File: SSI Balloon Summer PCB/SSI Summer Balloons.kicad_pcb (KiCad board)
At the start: 4 copper layers, 80 x 59 mm, 106 parts, among them J1 Battery connector, J2 Conn_01x02, J3 LoRa antenna, J4 APRS antenna, J5 Conn_01x05, J6 1040310811, J7 GPS antenna, J8 PT1000 Sensor, J9 Camera, Q2 DMG2305UX-7, SW2 SW_SPST, SW3 SW_SPST, U1 RFM95W-915S2, U10 MS5611-01BA03, U11 TPS63070RNMR, U12 TPS63070RNMR, U3 AP2112K-3.3TRG1, U4 ICM-42688-P, U5 DRA818V, U7 STM32F411CEUx, U8 MAX-M10S-00B, U9 MAX31865ATP_T, Y1 ABM8W-12.0000MHZ-8-K1Z-T3

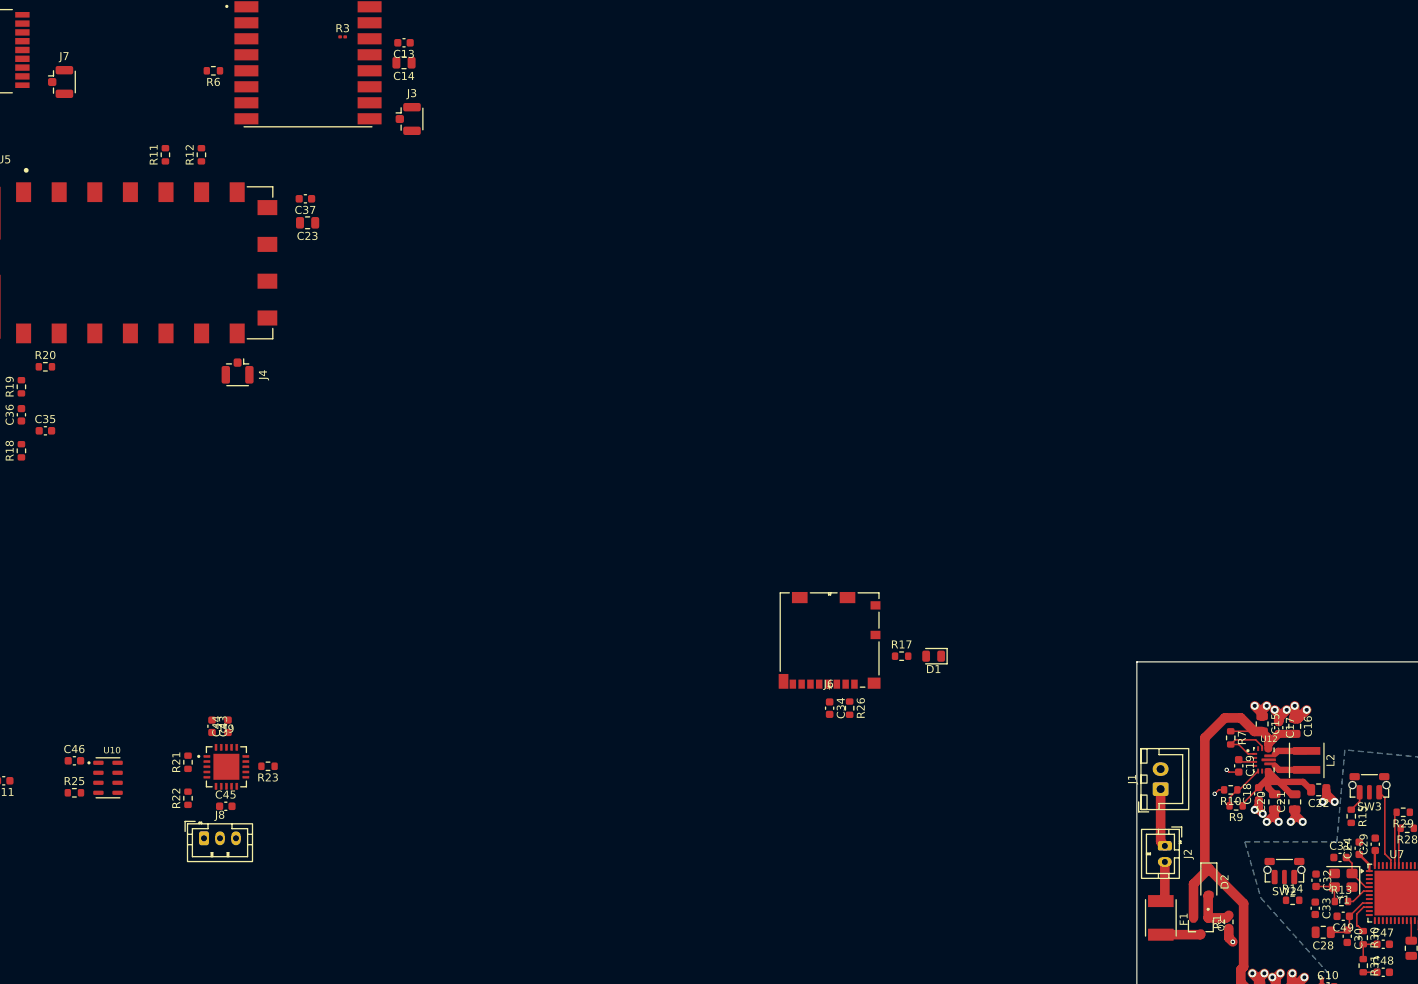
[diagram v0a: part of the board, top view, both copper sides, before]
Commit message: fixed footprints
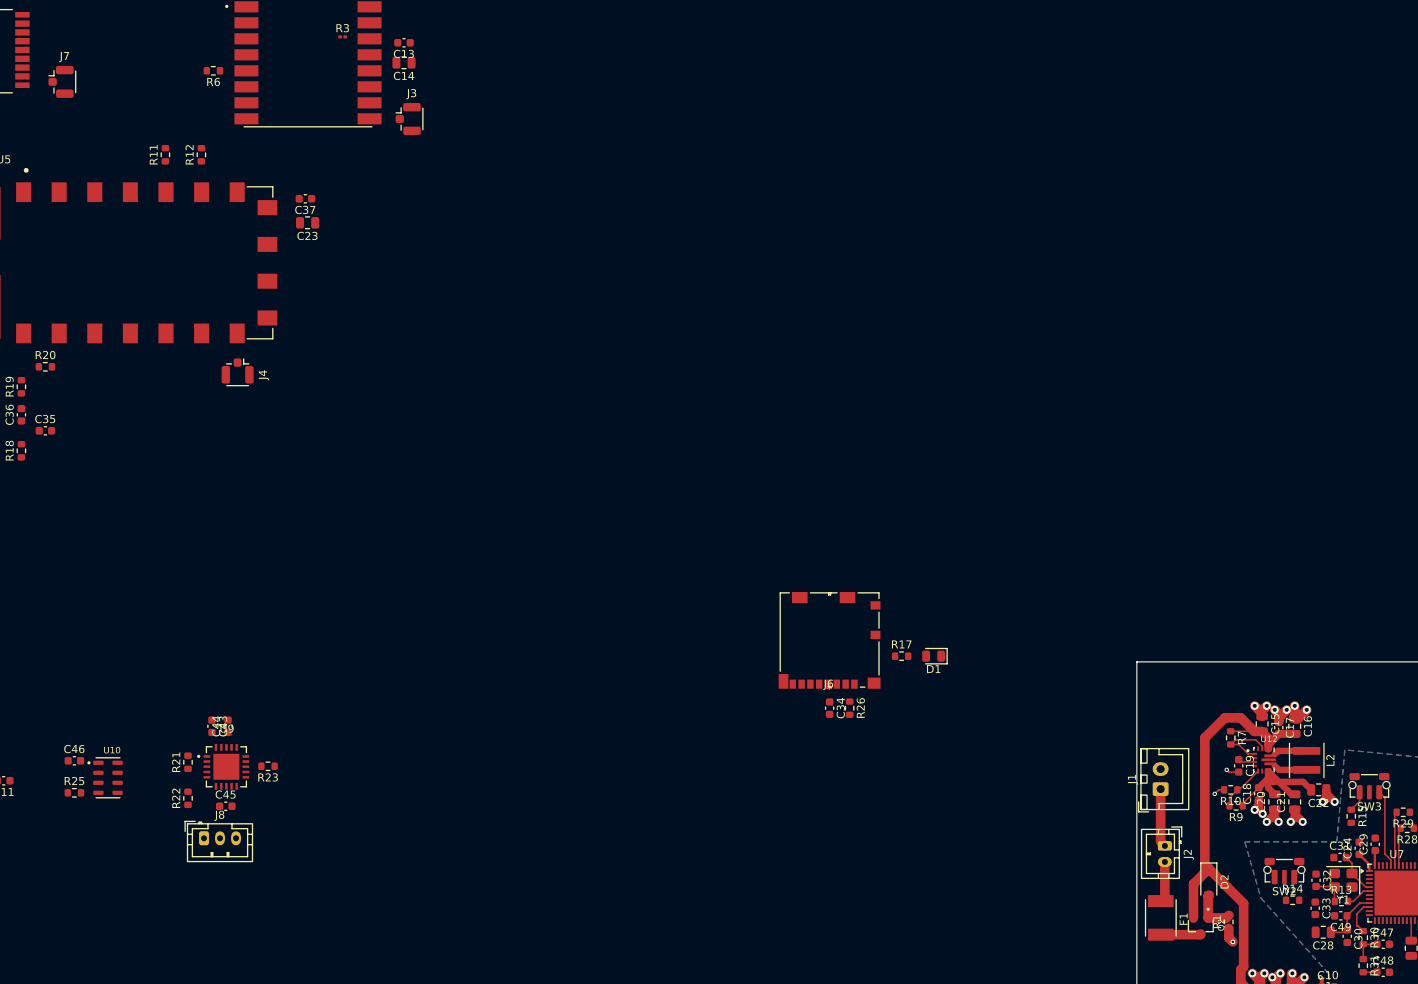
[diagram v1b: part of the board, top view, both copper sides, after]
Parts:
- moved C49 0.30 mm to (125.5, 110.2)
- moved J7 0.06 mm to (-34.0, 6.00)
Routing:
- net +3V3: track 19.0 -> 19.6 mm
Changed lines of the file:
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@@
 		)
 	)
-	(footprint "Capacitor_SMD:C_0603_1608Metric"
-		(layer "F.Cu")
-		(at 125.8 110.3 180)
-		(descr "Capacitor SMD 0603 (1608 Metric), square (rectangular) end terminal, IPC-7351 nominal, (Body size source: IPC-SM-782 page 76, https://www.pcb-3d.com/wordpress/wp-content/uploads/ipc-sm-782a_amendment_1_and_2.pdf)")
-		(tags "capacitor")
-		(property "Reference" "C49"
-			(at 0 -1.43 0)
-			(layer "F.SilkS")
-			(effects
-				(font
-					(size 1 1)
-					(thickness 0.15)
-				)
-			)
-		)
-		(property "Value" "100nF"
-			(at 0 1.43 0)
-			(layer "F.Fab")
-			(effects
-				(font
-					(size 1 1)
-					(thickness 0.15)
-				)
-			)
-		)
-		(property "Datasheet" ""
-			(at 0 0 0)
-			(layer "F.Fab")
-			(hide yes)
-			(effects
-				(font
-					(size 1.27 1.27)
-				)
-			)
-		)
-		(property "Description" "Unpolarized capacitor"
-			(at 0 0 0)
-			(layer "F.Fab")
-			(hide yes)
-			(effects
-				(font
-					(size 1.27 1.27)
-				)
-			)
-		)
-		(property "KiLib_Generator" "SMD_2terminal_chip_molded"
-			(at 0 0 0)
-			(layer "F.SilkS")
-			(hide yes)
-			(effects
-				(font
-					(size 1 1)
-					(thickness 0.15)
-				)
-			)
-		)
-		(property ki_fp_filters "C_*")
-		(sheetname "/MCU (STM)/")
-		(sheetfile "MCU.kicad_sch")
-		(units
-			(unit
-				(name "A")
-				(pins "1" "2")
-			)
-		)
-		(attr smd)
-		(duplicate_pad_numbers_are_jumpers no)
-		(fp_line
-			(start -0.14058 0.51)
-			(end 0.14058 0.51)
-			(stroke
-				(width 0.12)
-				(type solid)
-			)
-			(layer "F.SilkS")
-		)
-		(fp_line
-			(start -0.14058 -0.51)
-			(end 0.14058 -0.51)
-			(stroke
-				(width 0.12)
-				(type solid)
-			)
-			(layer "F.SilkS")
-		)
-		(fp_rect
-			(start -1.48 -0.73)
-			(end 1.48 0.73)
-			(stroke
-				(width 0.05)
-				(type solid)
-			)
-			(fill no)
-			(layer "F.CrtYd")
-		)
-		(fp_rect
-			(start -0.8 -0.4)
-			(end 0.8 0.4)
-			(stroke
-				(width 0.1)
-				(type solid)
-			)
-			(fill no)
-			(layer "F.Fab")
-		)
-		(fp_text user "${REFERENCE}"
-			(at 0 0 0)
-			(layer "F.Fab")
-			(effects
-				(font
-					(size 0.4 0.4)
-					(thickness 0.06)
-				)
-			)
-		)
-		(pad "1" smd roundrect
-			(at -0.775 0 180)
-			(size 0.9 0.95)
-			(layers "F.Cu" "F.Mask" "F.Paste")
-			(roundrect_rratio 0.25)
-			(net "+3V3")
-			(pintype "passive")
-		)
-		(pad "2" smd roundrect
-			(at 0.775 0 180)
-			(size 0.9 0.95)
-			(layers "F.Cu" "F.Mask" "F.Paste")
-			(roundrect_rratio 0.25)
-			(net "GND")
-			(pintype "passive")
-		)
-		(embedded_fonts no)
-		(model "${KICAD10_3DMODEL_DIR}/Capacitor_SMD.3dshapes/C_0603_1608Metric.step"
-			(offset
-				(xyz 0 0 0)
-			)
-			(scale
-				(xyz 1 1 1)
-			)
-			(rotate
-				(xyz 0 0 0)
-			)
-		)
-	)
 	(footprint "Resistor_SMD:R_0603_1608Metric"
 		(layer "F.Cu")
@@
 	(footprint "Connector_Coaxial:U.FL_Hirose_U.FL-R-SMT-1_Vertical"
 		(layer "F.Cu")
-		(at -34.055 6.015)
+		(at -34 6)
 		(descr "Hirose U.FL Coaxial (https://www.hirose.com/en/product/document?clcode=CL0331-0472-2-01&productname=U.FL-R-SMT-1(01)&series=U.FL&documenttype=2DDrawing&lang=en&documentid=0000940668)")
 		(tags "Hirose U.FL Coaxial")
@@
 			(polygon
 				(pts
-					(xy -32.955 5.065) (xy -35.045 5.065) (xy -35.045 6.965) (xy -32.955 6.965)
+					(xy -32.9 5.05) (xy -34.99 5.05) (xy -34.99 6.95) (xy -32.9 6.95)
 				)
 			)
@@
 		)
 	)
+	(footprint "Capacitor_SMD:C_0603_1608Metric"
+		(layer "F.Cu")
+		(at 125.5 110.245 180)
+		(descr "Capacitor SMD 0603 (1608 Metric), square (rectangular) end terminal, IPC-7351 nominal, (Body size source: IPC-SM-782 page 76, https://www.pcb-3d.com/wordpress/wp-content/uploads/ipc-sm-782a_amendment_1_and_2.pdf)")
+		(tags "capacitor")
+		(property "Reference" "C49"
+			(at 0 -1.43 0)
+			(layer "F.SilkS")
+			(effects
+				(font
+					(size 1 1)
+					(thickness 0.15)
+				)
+			)
+		)
+		(property "Value" "100nF"
+			(at 0 1.43 0)
+			(layer "F.Fab")
+			(effects
+				(font
+					(size 1 1)
+					(thickness 0.15)
+				)
+			)
+		)
+		(property "Datasheet" ""
+			(at 0 0 0)
+			(layer "F.Fab")
+			(hide yes)
+			(effects
+				(font
+					(size 1.27 1.27)
+				)
+			)
+		)
+		(property "Description" "Unpolarized capacitor"
+			(at 0 0 0)
+			(layer "F.Fab")
+			(hide yes)
+			(effects
+				(font
+					(size 1.27 1.27)
+				)
+			)
+		)
+		(property ki_fp_filters "C_*")
+		(sheetname "/MCU (STM)/")
+		(sheetfile "MCU.kicad_sch")
+		(units
+			(unit
+				(name "A")
+				(pins "1" "2")
+			)
+		)
+		(attr smd)
+		(duplicate_pad_numbers_are_jumpers no)
+		(fp_line
+			(start -0.14058 0.51)
+			(end 0.14058 0.51)
+			(stroke
+				(width 0.12)
+				(type solid)
+			)
+			(layer "F.SilkS")
+		)
+		(fp_line
+			(start -0.14058 -0.51)
+			(end 0.14058 -0.51)
+			(stroke
+				(width 0.12)
+				(type solid)
+			)
+			(layer "F.SilkS")
+		)
+		(fp_rect
+			(start -1.48 -0.73)
+			(end 1.48 0.73)
+			(stroke
+				(width 0.05)
+				(type solid)
+			)
+			(fill no)
+			(layer "F.CrtYd")
+		)
+		(fp_rect
+			(start -0.8 -0.4)
+			(end 0.8 0.4)
+			(stroke
+				(width 0.1)
+				(type solid)
+			)
+			(fill no)
+			(layer "F.Fab")
+		)
+		(fp_text user "${REFERENCE}"
+			(at 0 0 0)
+			(layer "F.Fab")
+			(effects
+				(font
+					(size 0.4 0.4)
+					(thickness 0.06)
+				)
+			)
+		)
+		(pad "1" smd roundrect
+			(at -0.775 0 180)
+			(size 0.9 0.95)
+			(layers "F.Cu" "F.Mask" "F.Paste")
+			(roundrect_rratio 0.25)
+			(net "+3V3")
+			(pintype "passive")
+		)
+		(pad "2" smd roundrect
+			(at 0.775 0 180)
+			(size 0.9 0.95)
+			(layers "F.Cu" "F.Mask" "F.Paste")
+			(roundrect_rratio 0.25)
+			(net "GND")
+			(pintype "passive")
+		)
+		(embedded_fonts no)
+		(model "${KICAD10_3DMODEL_DIR}/Capacitor_SMD.3dshapes/C_0603_1608Metric.step"
+			(offset
+				(xyz 0 0 0)
+			)
+			(scale
+				(xyz 1 1 1)
+			)
+			(rotate
+				(xyz 0 0 0)
+			)
+		)
+	)
 	(footprint "Resistor_SMD:R_0603_1608Metric"
 		(layer "F.Cu")
@@
 	)
 	(segment
-		(start 126.575 110.3)
-		(end 128.225 108.65)
-		(width 0.2)
-		(layer "F.Cu")
-		(net "+3V3")
-	)
-	(segment
-		(start 128.225 108.65)
-		(end 129.0625 108.65)
+		(start 126.025 112.3)
+		(end 126.3 112.025)
 		(width 0.2)
 		(layer "F.Cu")
@@
 	)
 	(segment
-		(start 126.025 112.3)
-		(end 126.3 112.025)
+		(start 126.275 110.245)
+		(end 126.275 112)
 		(width 0.2)
 		(layer "F.Cu")
@@
 	)
 	(segment
-		(start 126.575 110.3)
-		(end 126.575 111.75)
-		(width 0.2)
-		(layer "F.Cu")
-		(net "+3V3")
-	)
-	(segment
 		(start 126.575 111.75)
 		(end 126.3 112.025)
@@
 	)
 	(segment
+		(start 126.275 112)
+		(end 126.3 112.025)
+		(width 0.2)
+		(layer "F.Cu")
+		(net "+3V3")
+	)
+	(segment
 		(start 129.0625 104.65)
 		(end 129.0625 103.8375)
@@
 	)
 	(segment
+		(start 127.87 108.65)
+		(end 126.275 110.245)
+		(width 0.2)
+		(layer "F.Cu")
+		(net "+3V3")
+	)
+	(segment
 		(start 124.9425 119.395)
 		(end 124.6675 119.12)
@@
 		(layer "F.Cu")
 		(net "+3V3")
+	)
+	(segment
+		(start 129.0625 108.65)
+		(end 127.87 108.65)
+		(width 0.2)
+		(layer "F.Cu")
+		(net "+3V3")

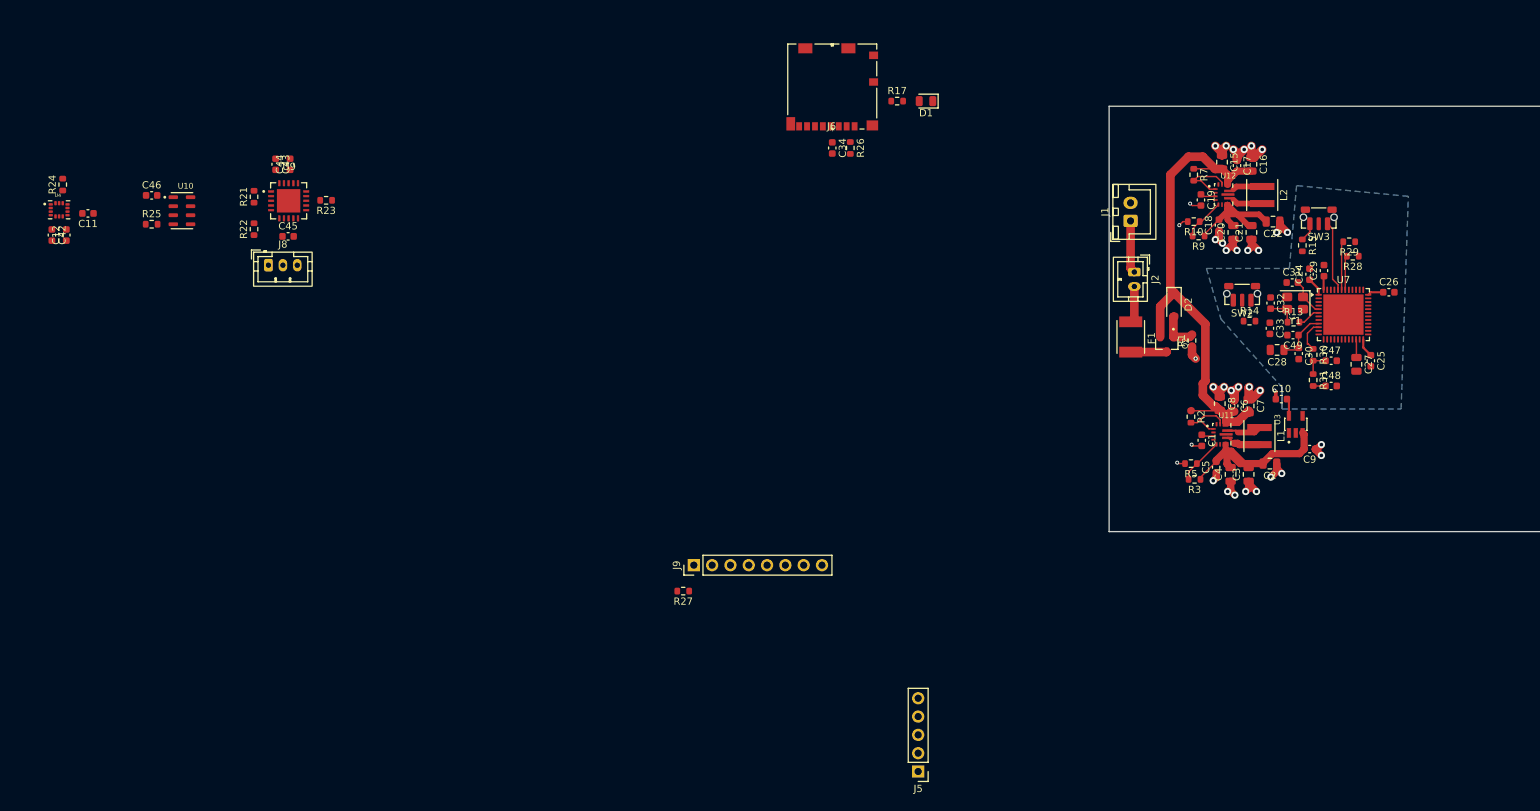
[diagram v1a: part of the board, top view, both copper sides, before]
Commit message: Routed IMU, Temp, Baro, SD
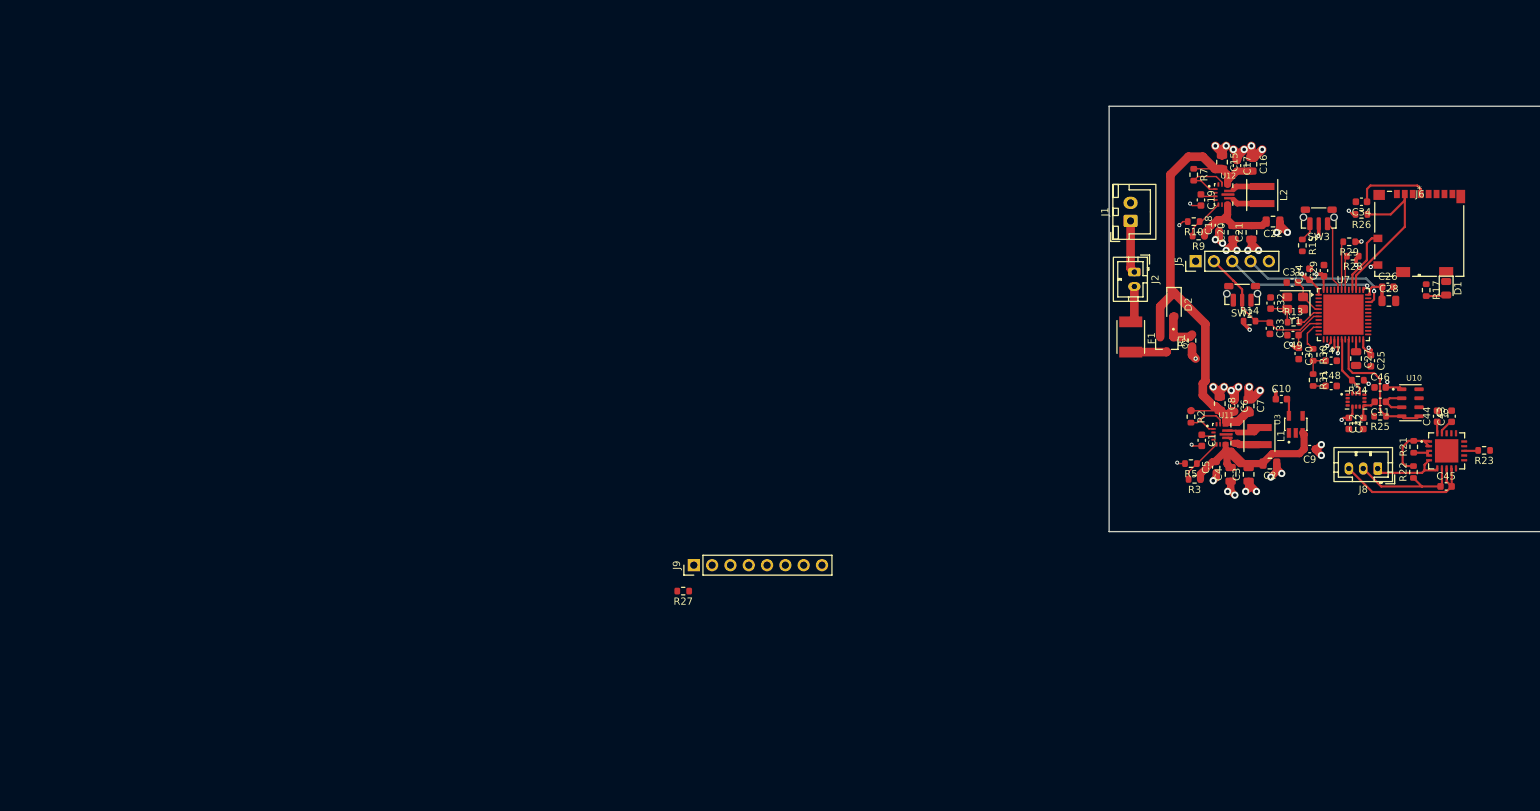
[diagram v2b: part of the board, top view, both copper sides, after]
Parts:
- moved U4 181.8 mm to (134.2, 119.2)
- moved C12 181.8 mm to (135.2, 122.5)
- moved C42 181.8 mm to (133.2, 122.5)
- moved R24 181.7 mm to (134.5, 116.5), turned to 180 degrees
- moved C11 181.1 mm to (137.6, 119.5)
- moved C46 172.5 mm to (137.6, 117.5)
- moved R25 172.5 mm to (137.6, 121.5), turned to 180 degrees
- moved U10 172.5 mm to (141.8, 119.6)
- moved C43 166.8 mm to (147.5, 121.5), turned to 90 degrees
- moved R21 164.6 mm to (142.2, 125.7)
- moved C45 164.3 mm to (146.7, 131.2)
- moved U9 164.3 mm to (146.8, 126.3)
- moved R23 164.3 mm to (152.0, 126.2)
- moved R22 164.3 mm to (142.2, 129.2)
- moved C44 162.9 mm to (145.5, 121.5)
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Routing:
- net +3V3: track 19.6 -> 57.8 mm, vias 0 -> 13
- net /MCU (STM)/microSD_CS: track 0.00 -> 23.0 mm
- net /MCU (STM)/SWDIO: track 0.00 -> 21.3 mm, vias 0 -> 1
- net Net-(J8-Pin_3): track 0.00 -> 21.2 mm
- net /MCU (STM)/SWCLK: track 0.00 -> 20.9 mm, vias 0 -> 1
- net /MCU (STM)/NRST: track 0.00 -> 20.7 mm
- net /MCU (STM)/BARO_CS: track 0.00 -> 19.3 mm
- net Net-(J8-Pin_2): track 0.00 -> 16.0 mm
- net Net-(J8-Pin_1): track 0.00 -> 10.4 mm
- net /Sensor/BIAS: track 0.00 -> 9.61 mm
- net /MCU (STM)/microSD_detect: track 0.00 -> 9.10 mm
- net /MCU (STM)/IMU_CS: track 0.00 -> 8.53 mm
- net +4V1: track 19.2 -> 13.2 mm
- net GND: track 58.8 -> 63.7 mm
- net Net-(U9-ISENSOR): track 0.00 -> 2.97 mm
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- added copper zone on In2.Cu, net +3V3
- removed copper zone on B.Cu, net +3V3

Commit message: Edits to PCB placement + traces - RF and GPS next
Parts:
- moved D1 17.0 mm to (134.2, 92.2), turned to 180 degrees
- moved R17 13.1 mm to (134.5, 95.0), turned to 180 degrees
- moved R25 12.4 mm to (145.5, 112.0), turned to 0 degrees
- moved C34 8.84 mm to (143.0, 88.0), turned to 90 degrees
- moved R26 8.14 mm to (141.0, 88.0), turned to 90 degrees
- moved C46 8.05 mm to (145.5, 116.0), turned to 180 degrees
- moved U10 5.63 mm to (141.5, 114.0), turned to 180 degrees
- moved C15 0.86 mm to (115.7, 85.4)
- moved C16 0.86 mm to (119.8, 85.7)
- moved C17 0.86 mm to (117.8, 85.9)
- moved C18 0.86 mm to (115.2, 94.1)
- moved C19 0.86 mm to (112.8, 90.6)
- moved C20 0.86 mm to (117.2, 95.1)
- moved C21 0.86 mm to (119.8, 95.1)
- moved C22 0.86 mm to (122.8, 93.6)
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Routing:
- net GND: track 63.7 -> 107.1 mm, vias 35 -> 67
- net /MCU (STM)/BARO_CS: track 19.3 -> 10.6 mm, vias 0 -> 2
- net /MCU (STM)/microSD_CS: track 23.0 -> 18.8 mm
- net /MCU (STM)/microSD_detect: track 9.10 -> 12.0 mm
- net VBAT_PROT: track 73.5 -> 74.7 mm
- net Net-(U7-PA0): track 4.48 -> 3.79 mm
- net /MCU (STM)/NRST: track 20.7 -> 21.0 mm, vias 0 -> 2
- net +3V3: track 57.8 -> 58.0 mm, vias 13 -> 18

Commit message: GPS and LoRa on PCB
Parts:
- removed the R3 at (0.72, 0.38)
- moved C39 236.2 mm to (162.5, 104.7), turned to 90 degrees
- moved C38 235.3 mm to (160.5, 104.8), turned to 90 degrees
- moved C40 234.3 mm to (158.5, 104.8), turned to 90 degrees
- moved C41 233.1 mm to (156.5, 104.5), turned to 90 degrees
- moved U8 221.8 mm to (157.0, 95.8), turned to 90 degrees
- moved J7 210.2 mm to (160.5, 85.7), turned to 90 degrees
- moved R12 207.0 mm to (97.2, 187.9), turned to 0 degrees
- moved R6 206.9 mm to (163.5, 108.5), turned to 0 degrees
- moved R11 205.9 mm to (97.2, 183.4), turned to 0 degrees
- moved C13 204.4 mm to (166.0, 131.2), turned to 90 degrees
- moved C37 204.0 mm to (91.7, 200.9), turned to 90 degrees
- moved U1 203.2 mm to (163.5, 119.2), turned to -90 degrees
- moved C14 200.8 mm to (163.5, 131.2), turned to 90 degrees
- moved C23 200.1 mm to (88.7, 201.2), turned to 90 degrees
- moved J3 190.8 mm to (156.5, 132.2), turned to -90 degrees
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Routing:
- net +3V3: track 58.0 -> 82.5 mm, vias 18 -> 19
- net GND: track 107.1 -> 123.2 mm, vias 67 -> 79
- net Net-(J7-In): track 0.00 -> 3.86 mm
- net Net-(J3-In): track 0.00 -> 3.79 mm
- net /MCU (STM)/LoRa_CS: track 0.00 -> 3.07 mm
- net +5V: track 28.3 -> 30.7 mm
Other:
- board size 80 x 59 mm -> 94.5 x 59 mm
